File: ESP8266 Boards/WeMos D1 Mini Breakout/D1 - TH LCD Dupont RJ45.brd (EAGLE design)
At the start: 44.1 x 44 mm, 19 parts, among them J1 RJ45-8X, Q1 2N7000, Q2 2N7000

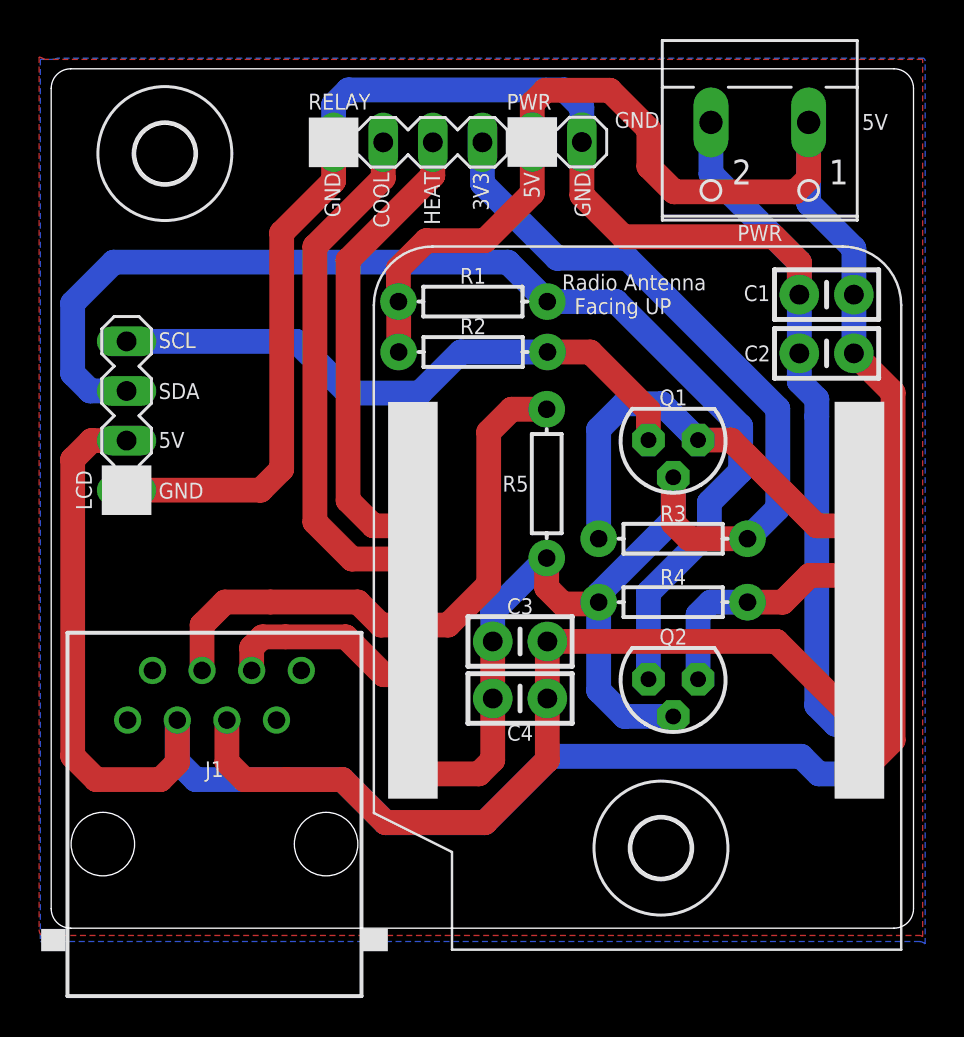
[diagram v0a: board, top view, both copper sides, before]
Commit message: Add voltage select header
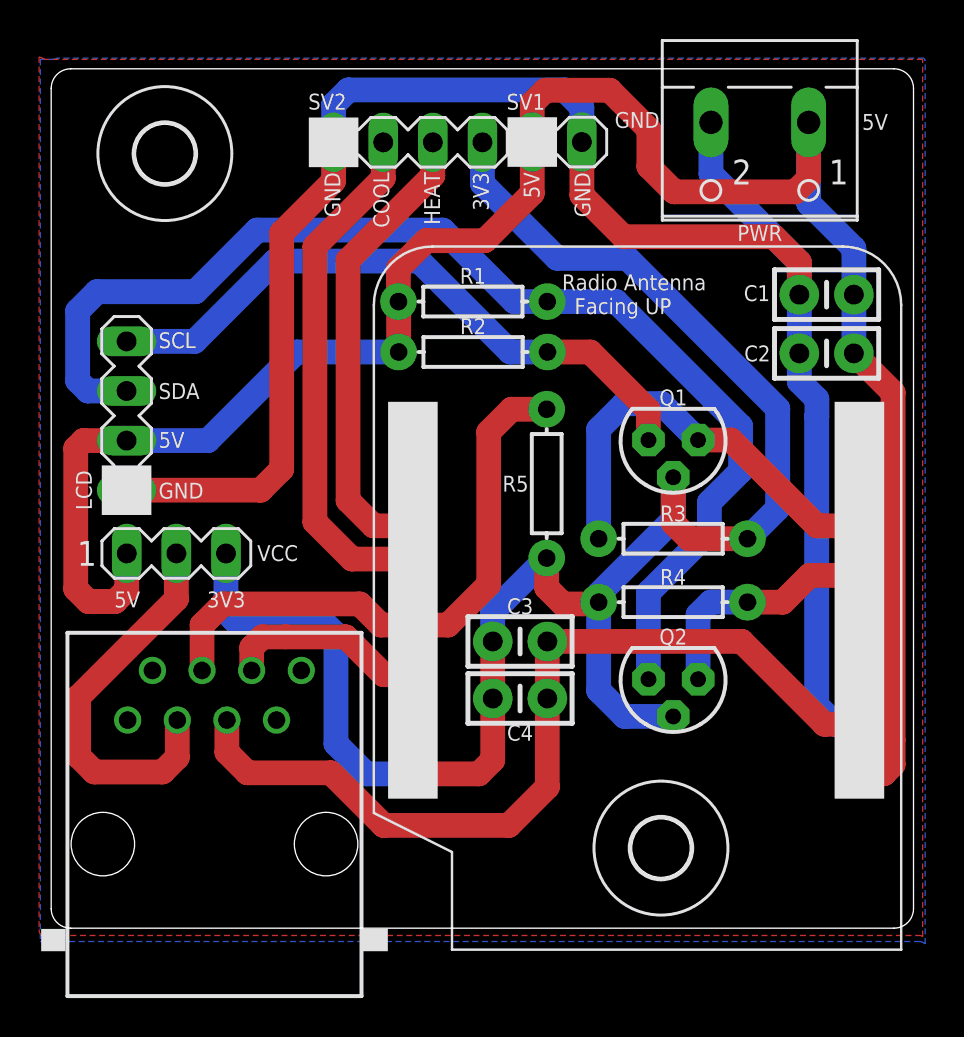
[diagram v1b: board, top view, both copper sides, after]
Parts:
- added VCC: SV3, con-lstb:MA03-1
- POWER: value PWR -> SV1
- RELAY: value RELAY -> SV2
- renumbered SV1 to RELAY, SV3 to POWER
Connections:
- new net VCC: J1.3, VCC.2
- net 3V3: now also VCC.3
- net 5V: now also VCC.1; no longer J1.3
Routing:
- net 5V: track 140.9 -> 105.5 mm
- net VCC: track 0.00 -> 20.1 mm
- net 3V3: track 73.1 -> 92.4 mm
- net 5VSCL: track 31.4 -> 33.1 mm
- net 5VSDA: track 60.2 -> 61.0 mm
- net GND: track 139.9 -> 140.5 mm
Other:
- board text added: "BrewPi D1 Mini Breakout Board v1.3.2 @LBussy on HBT"
- board text added: "RJ45: 3 - VCC 4 - OneWire 5 - Ground 6 - Door"
- board text removed: "BrewPi D1 Mini Breakout Board v1.3.1b @LBussy on HBT"
- board text removed: "RJ45: 3 - 5V 4 - OneWire 5 - Ground 6 - Door"

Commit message: Fix pour and links
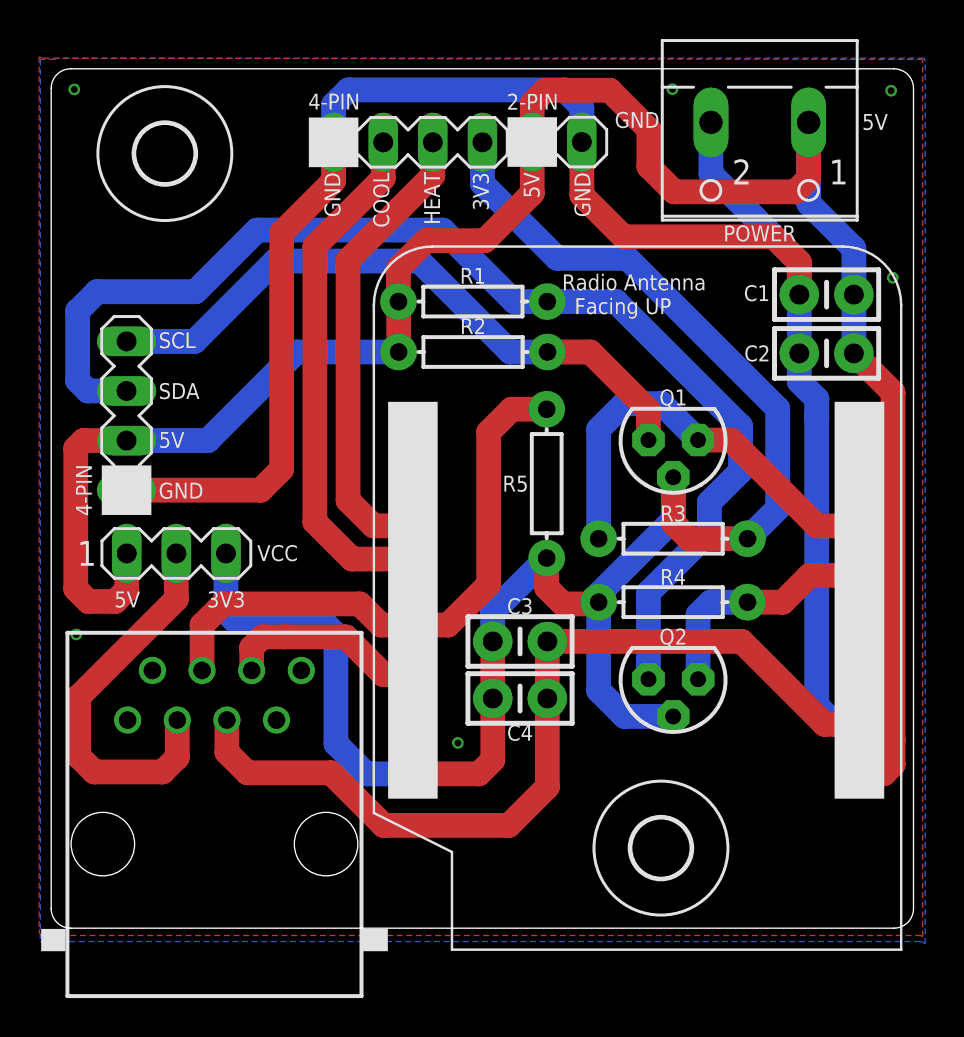
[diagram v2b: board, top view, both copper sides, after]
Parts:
- removed X: PWR, con-wago-500:W237-102
- added RPOWER: 2-PIN, Donnie:HDR-2_VERT
- LCD: value LCD -> 4-PIN
- POWER: value SV1 -> PWR; device Donnie:HDR-2_VERT -> con-wago-500:W237-102
- RELAY: value SV2 -> 4-PIN
- VCC: value SV3 -> 3-PIN
- moved POWER 11.7 mm to (36.3, 40.0), turned to 180 degrees
- renumbered SV2 to LCD
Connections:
- net 5V: now also RPOWER.1; no longer X.1
- net GND: now also RPOWER.2; no longer X.2
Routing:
- net GND: vias 0 -> 6
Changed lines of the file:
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@@
 <setting verticaltext="up"/>
 </settings>
-<grid distance="0.15" unitdist="mil" unit="mil" style="lines" multiple="1" display="yes" altdistance="0.01" altunitdist="mm" altunit="mm"/>
+<grid distance="0.15" unitdist="mil" unit="mm" style="lines" multiple="1" display="yes" altdistance="0.01" altunitdist="mm" altunit="mm"/>
 <layers>
 <layer number="1" name="Top" color="4" fill="1" visible="yes" active="yes"/>
@@
 &lt;a href=&quot;http://docs.oshpark.com/design-tools/eagle/design-rules-files/&quot;&gt;Adjustable Settings&lt;/a&gt;
 &lt;/p&gt;</description>
-<param name="layerSetup" value="1*16"/>
+<param name="layerSetup" value="(1*16)"/>
 <param name="mtCopper" value="0.035559375mm 0.0356mm 0.0356mm 0.0356mm 0.0356mm 0.0356mm 0.0356mm 0.0356mm 0.0356mm 0.0356mm 0.0356mm 0.0356mm 0.0356mm 0.0356mm 0.0356mm 0.035559375mm"/>
 <param name="mtIsolate" value="1.6mm 0.1499mm 0.2007mm 0.1499mm 0.2007mm 0.1499mm 0.2007mm 0.1499mm 0.2007mm 0.1499mm 0.2007mm 0.1499mm 0.2007mm 0.1499mm 0.2007mm"/>
@@
 <param name="mlMinCreamFrame" value="0mil"/>
 <param name="mlMaxCreamFrame" value="0mil"/>
-<param name="mlViaStopLimit" value="0mil"/>
+<param name="mlViaStopLimit" value="30mil"/>
 <param name="srRoundness" value="0"/>
 <param name="srMinRoundness" value="0mil"/>
@@
 <elements>
 <element name="U$1" library="Wemos" package="WEMOS_D1-NOTEXT" value="WEMOSNOTEXT" x="18.52" y="7.9" smashed="yes"/>
-<element name="X" library="con-wago-500" package="W237-102" value="PWR" x="36.28" y="39.985" smashed="yes" rot="R180">
+<element name="POWER" library="con-wago-500" package="W237-102" value="PWR" x="36.28" y="39.985" smashed="yes" rot="R180">
 <attribute name="MF" value="" x="36.28" y="39.985" size="0.8128" layer="27" rot="R180" display="off"/>
 <attribute name="MPN" value="237-102" x="36.28" y="39.985" size="0.8128" layer="27" rot="R180" display="off"/>
+<attribute name="NAME" x="36.274290625" y="35.97815" size="0.8128" layer="25" font="vector" align="top-center"/>
 <attribute name="OC_FARNELL" value="unknown" x="36.28" y="39.985" size="0.8128" layer="27" rot="R180" display="off"/>
 <attribute name="OC_NEWARK" value="70K9898" x="36.28" y="39.985" size="0.8128" layer="27" rot="R180" display="off"/>
-<attribute name="VALUE" x="36.28" y="36" size="0.8128" layer="25" font="vector" rot="R180" align="bottom-center"/>
 </element>
 <element name="J1" library="con-tycoelectronics" package="RJ45-NO-SHIELD-NOLINE" value="RJ45-8X" x="8.36" y="4.305" smashed="yes">
@@
 <element name="U$2" library="holes" package="3,0" value="" x="5.82" y="39.66" smashed="yes"/>
 <element name="U$4" library="holes" package="3,0" value="" x="31.22" y="4.1" smashed="yes"/>
-<element name="RELAY" library="Donnie" package="HDR-4_VERT" value="SV2" x="14.46" y="40.235" smashed="yes">
+<element name="RELAY" library="Donnie" package="HDR-4_VERT" value="4-PIN" x="14.46" y="40.235" smashed="yes">
 <attribute name="VALUE" x="13.16" y="41.913" size="0.8128" layer="25" font="vector"/>
 </element>
-<element name="SV2" library="Donnie" package="HDR-4_VERT" value="LCD" x="3.86" y="22.425" smashed="yes" rot="R90">
+<element name="LCD" library="Donnie" package="HDR-4_VERT" value="4-PIN" x="3.86" y="22.425" smashed="yes" rot="R90">
 <attribute name="VALUE" x="2.082" y="22.425" size="0.8128" layer="25" font="vector" rot="R90" align="bottom-center"/>
 </element>
@@
 <attribute name="NAME" x="36.822" y="29.427" size="0.8128" layer="25" font="vector" align="center-right"/>
 </element>
-<element name="POWER" library="Donnie" package="HDR-2_VERT" value="SV1" x="24.63" y="40.25" smashed="yes">
+<element name="RPOWER" library="Donnie" package="HDR-2_VERT" value="2-PIN" x="24.63" y="40.25" smashed="yes">
 <attribute name="VALUE" x="23.32" y="41.905" size="0.8128" layer="25" font="vector"/>
 </element>
-<element name="VCC" library="con-lstb" library_urn="urn:adsk.eagle:library:162" package="MA03-1" package3d_urn="urn:adsk.eagle:package:8339/1" value="SV3" x="6.408425" y="19.187159375" smashed="yes">
+<element name="VCC" library="con-lstb" library_urn="urn:adsk.eagle:library:162" package="MA03-1" package3d_urn="urn:adsk.eagle:package:8339/1" value="3-PIN" x="6.408425" y="19.187159375" smashed="yes">
 <attribute name="MF" value="" x="6.408425" y="19.187159375" size="1.778" layer="27" display="off"/>
 <attribute name="MPN" value="" x="6.408425" y="19.187159375" size="1.778" layer="27" display="off"/>
@@
 <signal name="GND" class="3">
 <contactref element="U$1" pad="GND"/>
-<contactref element="X" pad="2"/>
+<contactref element="POWER" pad="2"/>
 <contactref element="RELAY" pad="1"/>
-<contactref element="SV2" pad="1"/>
+<contactref element="LCD" pad="1"/>
 <contactref element="C1" pad="1"/>
 <contactref element="J1" pad="5"/>
@@
 <contactref element="C3" pad="2"/>
 <wire x1="35.356921875" y1="14.68" x2="39.596921875" y2="10.44" width="1.27" layer="1"/>
-<contactref element="POWER" pad="2"/>
+<contactref element="RPOWER" pad="2"/>
 <wire x1="39.596921875" y1="10.44" x2="41.38" y2="10.44" width="1.27" layer="1"/>
 <wire x1="27.17" y1="40.25" x2="27.17" y2="37.53" width="1.27" layer="1"/>
@@
 <wire x1="39.2" y1="26.2" x2="39.2" y2="27.0908" width="1.27" layer="16"/>
 <wire x1="39.2" y1="27.0908" x2="38.303" y2="27.9878" width="1.27" layer="16"/>
-<polygon width="1.27" layer="1">
+<polygon width="1.27" layer="1" orphans="yes">
 <vertex x="-0.62103125" y="44.60748125"/>
 <vertex x="-0.62103125" y="-0.069840625" curve="45"/>
@@
 <vertex x="44.618909375" y="-0.434340625"/>
 <vertex x="44.618909375" y="44.48175"/>
-<vertex x="-0.287171875" y="44.48175" curve="-45"/>
 <vertex x="-0.434340625" y="44.542709375"/>
 </polygon>
-<polygon width="1.27" layer="16">
+<polygon width="1.27" layer="16" orphans="yes">
 <vertex x="-0.556259375" y="44.48175"/>
 <vertex x="-0.556259375" y="-0.681990625"/>
@@
 <wire x1="17.019271875" y1="5.261609375" x2="23.435309375" y2="5.261609375" width="1.27" layer="1"/>
 <wire x1="23.435309375" y1="5.261609375" x2="25.402" y2="7.2283" width="1.27" layer="1"/>
+<via x="1.28396875" y="15.03806875" extent="1-16" drill="0.35"/>
+<via x="20.82165" y="9.4869" extent="1-16" drill="0.35"/>
+<via x="31.809690625" y="42.953940625" extent="1-16" drill="0.35"/>
+<via x="43.087290625" y="33.303209375" extent="1-16" drill="0.35"/>
+<via x="43.00346875" y="42.877740625" extent="1-16" drill="0.35"/>
+<via x="1.1811" y="42.942509375" extent="1-16" drill="0.35"/>
 </signal>
 <signal name="5V" class="1">
 <contactref element="U$1" pad="5V"/>
-<contactref element="X" pad="1"/>
-<contactref element="SV2" pad="2"/>
+<contactref element="POWER" pad="1"/>
+<contactref element="LCD" pad="2"/>
 <contactref element="C1" pad="2"/>
 <contactref element="R2" pad="P$1"/>
@@
 <wire x1="43.1058" y1="9.6258" x2="43.1058" y2="27.4212" width="1.27" layer="1"/>
 <contactref element="C2" pad="2"/>
-<contactref element="POWER" pad="1"/>
+<contactref element="RPOWER" pad="1"/>
 <wire x1="17.78065" y1="32.081984375" x2="17.78065" y2="33.78065" width="1.27" layer="1"/>
 <wire x1="19.2" y1="35.2" x2="22.2" y2="35.2" width="1.27" layer="1"/>
@@
 </signal>
 <signal name="5VSCL">
-<contactref element="SV2" pad="4"/>
+<contactref element="LCD" pad="4"/>
 <contactref element="R2" pad="P$2"/>
 <contactref element="Q1" pad="3"/>
@@
 </signal>
 <signal name="5VSDA">
-<contactref element="SV2" pad="3"/>
+<contactref element="LCD" pad="3"/>
 <contactref element="R1" pad="P$2"/>
 <contactref element="Q2" pad="3"/>
